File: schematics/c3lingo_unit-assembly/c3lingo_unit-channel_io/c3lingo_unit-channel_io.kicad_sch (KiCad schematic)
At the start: 38 parts, among them J801 Mic X In, J802 Headphone X, J803 Interconnect, J804 PowerSupply, U801 NE5534, U802 TPA6111A2

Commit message: Tidy: Rename hierarchical labels
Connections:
- net HeadphoneAmpIn renamed Headphone
- net MicPreOut renamed MicPre
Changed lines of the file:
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@@
 		)
 	)
-	(hierarchical_label "MicPreOut"
+	(hierarchical_label "MicPre"
 		(shape output)
 		(at 127 76.2 0)
@@
 		)
 	)
-	(hierarchical_label "HeadphoneAmpIn"
+	(hierarchical_label "Headphone"
 		(shape input)
 		(at 173.99 76.2 180)
@@
 		)
 	)
-	(hierarchical_label "MicPreOut"
+	(hierarchical_label "MicPre"
 		(shape output)
 		(at 66.04 177.8 0)
@@
 		)
 	)
-	(hierarchical_label "HeadphoneAmpIn"
+	(hierarchical_label "Headphone"
 		(shape input)
 		(at 66.04 180.34 0)

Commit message: Channel Mixer: Rework muting mechanism
Note: Schematic PDF not updated yet
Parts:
- C802, C807: footprint Capacitor_SMD:C_Elec_6.3x7.7 -> Capacitor_SMD:CP_Elec_6.3x7.7
- C805, C809, C810, C811, C814: footprint Capacitor_SMD:C_Elec_4x5.8 -> Capacitor_SMD:CP_Elec_4x5.8
- C806, C808: footprint Capacitor_SMD:C_Elec_6.3x5.8 -> Capacitor_SMD:CP_Elec_6.3x5.8
- R802, R808: value 330K 1% -> 68K 1%
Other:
- note added: "Mic Preamp Gain: 35 dB"
- note removed: "Mic Preamp Gain: 50 dB"
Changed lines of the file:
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@@
 	(title_block
 		(title "c3lingo interpeter unit -- channel strip (I/O)")
-		(date "2024-07-08")
+		(date "2024-08-30")
 		(rev "v0.3.1")
 		(company "Jannik Beyerstedt (jtbx)")
@@
 		)
 	)
-	(text "Mic Preamp\nGain: 50 dB"
+	(text "Mic Preamp\nGain: 35 dB"
 		(exclude_from_sim no)
 		(at 71.12 101.6 0)
@@
 			)
 		)
-		(property "Value" "330K 1%"
+		(property "Value" "68K 1%"
 			(at 106.68 85.9536 90)
 			(effects
@@
 			)
 		)
-		(property "Value" "330K 1%"
+		(property "Value" "68K 1%"
 			(at 106.68 60.5536 90)
 			(effects
@@
 			)
 		)
-		(property "Footprint" "Capacitor_SMD:C_Elec_4x5.8"
+		(property "Footprint" "Capacitor_SMD:CP_Elec_4x5.8"
 			(at 228.6 107.6452 0)
 			(effects
@@
 			)
 		)
-		(property "Footprint" "Capacitor_SMD:C_Elec_6.3x5.8"
+		(property "Footprint" "Capacitor_SMD:CP_Elec_6.3x5.8"
 			(at 252.73 80.3148 0)
 			(effects
@@
 			)
 		)
-		(property "Footprint" "Capacitor_SMD:C_Elec_6.3x5.8"
+		(property "Footprint" "Capacitor_SMD:CP_Elec_6.3x5.8"
 			(at 252.73 85.3948 0)
 			(effects
@@
 			)
 		)
-		(property "Footprint" "Capacitor_SMD:C_Elec_6.3x7.7"
+		(property "Footprint" "Capacitor_SMD:CP_Elec_6.3x7.7"
 			(at 54.9148 82.55 0)
 			(effects
@@
 			)
 		)
-		(property "Footprint" "Capacitor_SMD:C_Elec_4x5.8"
+		(property "Footprint" "Capacitor_SMD:CP_Elec_4x5.8"
 			(at 48.26 62.5348 0)
 			(effects
@@
 			)
 		)
-		(property "Footprint" "Capacitor_SMD:C_Elec_4x5.8"
+		(property "Footprint" "Capacitor_SMD:CP_Elec_4x5.8"
 			(at 185.42 82.2452 0)
 			(effects
@@
 			)
 		)
-		(property "Footprint" "Capacitor_SMD:C_Elec_4x5.8"
+		(property "Footprint" "Capacitor_SMD:CP_Elec_4x5.8"
 			(at 48.26 87.9348 0)
 			(effects
@@
 			)
 		)
-		(property "Footprint" "Capacitor_SMD:C_Elec_6.3x7.7"
+		(property "Footprint" "Capacitor_SMD:CP_Elec_6.3x7.7"
 			(at 243.84 50.4952 0)
 			(effects
@@
 			)
 		)
-		(property "Footprint" "Capacitor_SMD:C_Elec_4x5.8"
+		(property "Footprint" "Capacitor_SMD:CP_Elec_4x5.8"
 			(at 185.42 87.3252 0)
 			(effects

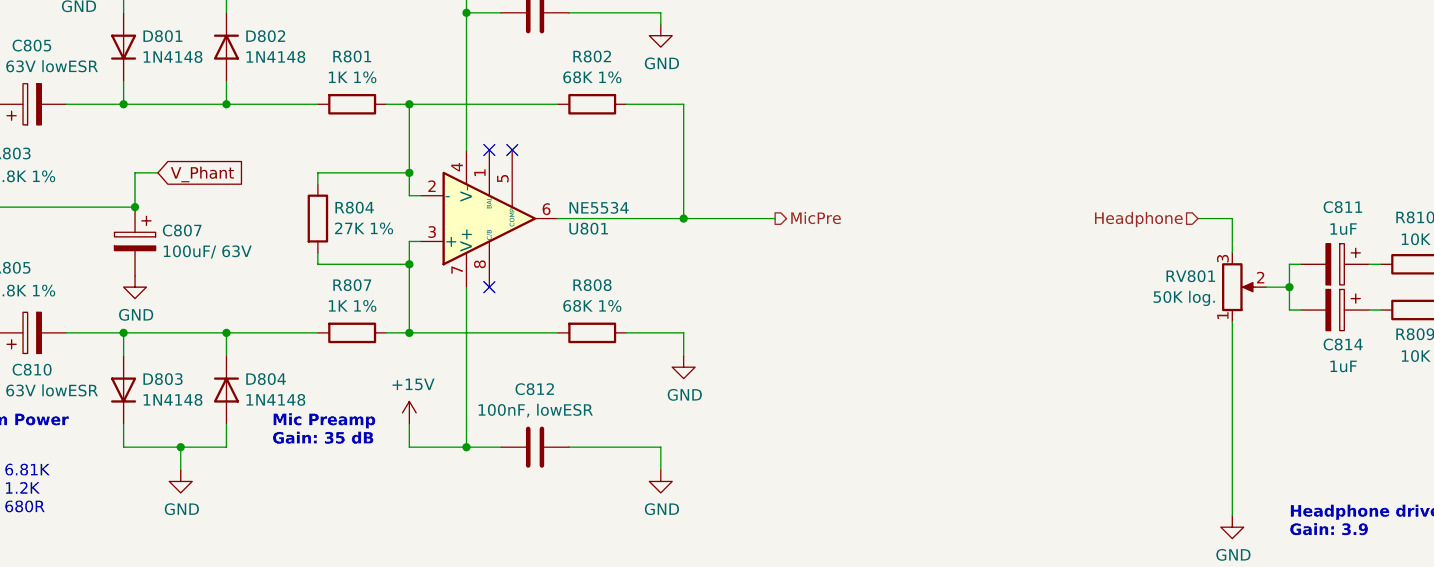
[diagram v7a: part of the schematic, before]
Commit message: Move potentiometers down, fix JLC PCB components
- Fix JLC PCB component orientation
- Add do-not-populate to all THD components
- Fix JLC part selection, tweak values to be standard components
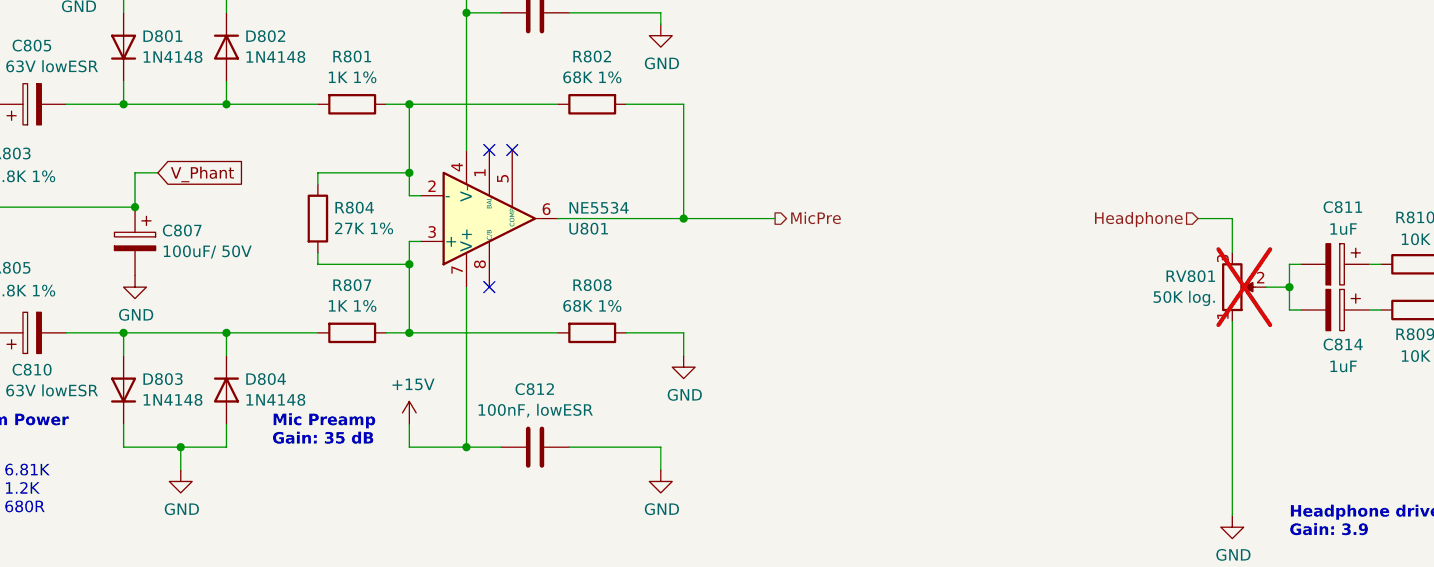
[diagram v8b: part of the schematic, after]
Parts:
- C802: footprint Capacitor_SMD:CP_Elec_6.3x7.7 -> Capacitor_SMD:CP_Elec_8x10; JLCPCB Rotation Offset (none) -> 180; LCSC Part # C72478 -> C116241
- C805, C809, C810, C811, C814, D801, D802, D803, D804: JLCPCB Rotation Offset (none) -> 180
- C806, C808: footprint Capacitor_SMD:CP_Elec_6.3x5.8 -> Capacitor_SMD:CP_Elec_5x5.8; JLCPCB Rotation Offset (none) -> 180; LCSC Part # C72478 -> C178592
- C807: value 100uF/ 63V -> 100uF/ 50V; footprint Capacitor_SMD:CP_Elec_6.3x7.7 -> Capacitor_SMD:CP_Elec_8x10; JLCPCB Rotation Offset (none) -> 180; LCSC Part # C72478 -> C116241
- R801, R807: LCSC Part # (none) -> C17513
- R802, R808: LCSC Part # (none) -> C17801
- R803, R805: LCSC Part # (none) -> C17772
- R804: LCSC Part # (none) -> C17593
- R806, R811: footprint Resistor_SMD:R_0805_2012Metric_Pad1.20x1.40mm_HandSolder -> Resistor_SMD:R_0603_1608Metric_Pad0.98x0.95mm_HandSolder; LCSC Part # (none) -> C23153
- RV801: now not fitted
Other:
- title: c3lingo interpeter unit -- channel strip (I/O) -> c3lingo interpeter unit -- channel I/O
